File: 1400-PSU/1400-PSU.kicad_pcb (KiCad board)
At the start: 2 copper layers, 173.4 x 62.1 mm, 42 parts, among them J1 Battery, J2 Charger, J3 MAINBOARD_OUT, Q1 IRF9540N, SW1 SW_DPST, U3 LM7805_TO220, U4 7812

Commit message: Generated gerbers.
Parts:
- added F1: 3A, Fuse:Fuseholder_Blade_Mini_Keystone_3568, F.Cu at (86.0, 76.7)
- added G***: LOGO, Logo:Logo-15mm, F.Cu at (192.6, 98.8)
- added NT1: NetTie_2, NetTie:NetTie-2_SMD_Pad2.0mm, F.Cu at (92.6, 93.0)
- added NT2: NetTie_2, NetTie:NetTie-2_SMD_Pad2.0mm, F.Cu at (88.2, 102.9)
- added NT3: NetTie_2, NetTie:NetTie-2_SMD_Pad2.0mm, F.Cu at (112.2, 92.9)
- C1: footprint Capacitor_THT:CP_Radial_D10.0mm_P5.00mm -> Capacitor_THT:CP_Radial_D8.0mm_P3.50mm
- C3: footprint Capacitor_THT:C_Disc_D4.7mm_W2.5mm_P5.00mm -> Capacitor_THT:C_Disc_D5.1mm_W3.2mm_P5.00mm
- C4: value 22uF 25V -> 0.1uF; footprint Capacitor_THT:CP_Radial_D6.3mm_P2.50mm -> Capacitor_THT:C_Disc_D5.1mm_W3.2mm_P5.00mm
- C8: value 10uF 50V -> 0.22uF; footprint Capacitor_THT:CP_Radial_D8.0mm_P5.00mm -> Capacitor_THT:C_Disc_D5.1mm_W3.2mm_P5.00mm
- J2: value Charger -> Jack-DC
- U3: footprint Package_TO_SOT_THT:TO-220-3_Vertical -> Package_TO_SOT_THT:TO-220-3_Horizontal_TabDown
- U4: value 7812 -> LM340T-12; footprint Package_TO_SOT_THT:TO-220-3_Vertical -> Package_TO_SOT_THT:TO-220-3_Horizontal_TabDown
- U5: value ~ -> N7812-1PH; footprint Package_TO_SOT_THT:TO-220-3_Vertical -> Package_TO_SOT_THT:TO-220-3_Horizontal_TabDown
- moved R1 84.2 mm to (92.3, 84.0), turned to 0 degrees
- moved R2 84.0 mm to (92.5, 88.2), turned to 0 degrees
- moved U2 82.0 mm to (180.6, 58.5)
- moved R8 81.9 mm to (165.2, 73.1)
- moved R9 81.9 mm to (175.1, 73.1)
- moved JP1 55.3 mm to (184.9, 117.3), turned to -90 degrees
- moved C8 54.5 mm to (113.7, 102.6)
- moved C7 41.0 mm to (148.6, 105.8), turned to 180 degrees
- moved C6 39.4 mm to (158.7, 112.8)
- moved U3 35.3 mm to (153.6, 106.7), turned to 0 degrees
- moved R6 31.8 mm to (119.9, 67.5)
- moved RV1 29.7 mm to (130.3, 68.8)
- moved U4 28.8 mm to (118.8, 107.0), turned to 0 degrees
- moved C2 27.2 mm to (96.1, 78.6)
- moved R4 26.7 mm to (119.9, 71.3)
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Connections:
- D1 pad 2: BATT_SENSE -> Net-(D1-A)
- J2 pad 1: GND -> Net-(F1-Pad2)
- J2 pad 2: POWER_BRICK -> GND
- Q1 pad 2: BATT_SENSE -> Net-(D1-A)
- R1 pad 2: POWER_BRICK -> Net-(NT1-Pad2)
- R2 pad 1: POWER_BRICK -> Net-(NT1-Pad2)
- R8 pad 1: POWER_BRICK -> CHARGER_SENSE
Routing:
- net 15_RAIL: track 144.3 -> 238.7 mm, vias 1 -> 0
- net Net-(A1-A1): track 136.5 -> 45.5 mm, vias 3 -> 0
- net POWER_BRICK: track 146.6 -> 58.4 mm, vias 1 -> 0
- net Net-(Q1-G): track 104.7 -> 27.2 mm, vias 3 -> 0
- net Net-(JP2-A): track 101.0 -> 39.3 mm
- net CHARGER_SENSE: track 0.00 -> 59.4 mm, vias 0 -> 1
- net 5_RAIL: track 74.0 -> 33.7 mm
- net Net-(D1-K): track 139.5 -> 110.0 mm, vias 8 -> 0
- net ARDUINO_5V: track 25.4 -> 52.9 mm, vias 0 -> 1
- net Net-(D1-A): track 0.00 -> 25.8 mm
- net 12_RAIL: track 88.5 -> 65.1 mm
- net LOW_BATT: track 40.6 -> 20.6 mm, vias 2 -> 0
- net BATT_SENSE: track 106.0 -> 86.2 mm, vias 2 -> 1
- net REALLY_LOW_BATT: track 41.3 -> 22.1 mm, vias 2 -> 0
- net STANDBY: track 43.4 -> 24.5 mm, vias 2 -> 0
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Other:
- board text added: "-12V_RAIL"
- board text added: "-22V_RAIL"
- board text added: "12V_RAIL"
- board text added: "5V_RAIL"
- board text added: "ALWAYS_ON_5V"
- board text added: "GND"
- board text added: "LOW_BATT"
- board text added: "NOT_CONNECTED"
- board text added: "ON_CHARGER"
- board text added: "OPTIONAL TP5100 CHARGER"
- board text added: "PWR_ON"
- board text added: "REALLY_LOW_BATT"
- board text added: "STANDBY"
- board text added: "TANDY 1400FD/HD PSU REAPLCEMENT"

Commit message: Updating for next board revision.
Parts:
- removed REF** (x4): MountingHole_3.5mm_Pad_TopBottom, MountingHole:MountingHole_3.5mm_Pad_TopBottom
- added H1: ~, MountingHole:MountingHole_3.5mm_Pad_TopBottom, F.Cu at (222.4, 63.6)
- added H2: ~, MountingHole:MountingHole_3.5mm_Pad_TopBottom, F.Cu at (197.5, 117.7)
- added H3: ~, MountingHole:MountingHole_3.5mm_Pad_TopBottom, F.Cu at (62.0, 115.1)
- added H4: ~, MountingHole:MountingHole_3.5mm_Pad_TopBottom, F.Cu at (74.7, 66.5)
- added JP3: LOW_BATT, Jumper:SolderJumper-2_P1.3mm_Open_RoundedPad1.0x1.5mm, F.Cu at (196.6, 81.6)
- added JP4: REALLY_LOW_BATT, Jumper:SolderJumper-2_P1.3mm_Open_RoundedPad1.0x1.5mm, F.Cu at (199.2, 81.6)
- C2: value 220uF 50V -> 47uF 50V
- D1: value 1N4001 -> 31DQ06; footprint Diode_THT:D_DO-41_SOD81_P10.16mm_Horizontal -> Diode_THT:D_DO-201AD_P5.08mm_Vertical_AnodeUp
- D2: value 1N4001 -> 31D106; footprint Diode_THT:D_DO-41_SOD81_P10.16mm_Horizontal -> Diode_THT:D_DO-201AD_P5.08mm_Vertical_KathodeUp
- D4: value 1N4001 -> 31DQ06; footprint Diode_THT:D_DO-41_SOD81_P10.16mm_Horizontal -> Diode_THT:D_DO-201AD_P12.70mm_Horizontal
- R4: value 1k -> 20k
- R6: value 20k -> 1k
- moved D1 9.03 mm to (76.6, 87.6), turned to 90 degrees
- moved RV1 5.59 mm to (125.0, 67.0), turned to 90 degrees
- moved L1 4.59 mm to (109.1, 67.4), turned to 180 degrees
- moved D2 4.58 mm to (84.9, 87.7), turned to 90 degrees
- moved NT3 4.50 mm to (109.0, 89.7)
- moved J1 3.46 mm to (62.2, 91.9), turned to -90 degrees
- moved D4 3.44 mm to (67.5, 94.2)
- moved U2 1.78 mm to (181.5, 60.0)
- moved A1 0.60 mm to (188.7, 87.0)
- moved R9 0.55 mm to (175.0, 73.6)
- moved R8 0.54 mm to (165.1, 73.6)
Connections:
- C3 pad 2: GND -> -22_RAIL
- L1 pad 1: Net-(D3-K) -> GND
- L1 pad 2: Net-(U1-Switch_Emiiter) -> Net-(D3-K)
- U1 pad 2: Net-(U1-Switch_Emiiter) -> Net-(D3-K)
- U1 pad 4: GND -> -22_RAIL
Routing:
- net -22_RAIL: track 115.2 -> 143.8 mm
- net Net-(U1-Switch_Emiiter): track 22.9 -> 0.00 mm, vias 1 -> 0
- net Net-(D3-K): track 4.94 -> 25.4 mm, vias 0 -> 1
- net Net-(A1-VIN): track 43.2 -> 61.0 mm, vias 1 -> 2
- net Net-(D1-A): track 25.8 -> 35.1 mm
- net POWER_BRICK: track 58.4 -> 50.9 mm
- net 15_RAIL: track 238.7 -> 231.5 mm
- net Net-(D1-K): track 110.0 -> 116.4 mm
- net REALLY_LOW_BATT: track 22.1 -> 28.0 mm
- net LOW_BATT: track 20.6 -> 23.3 mm
- net BATT_SENSE: track 86.2 -> 88.8 mm, vias 1 -> 3
- net Net-(JP2-A): track 39.3 -> 41.2 mm
- net CHARGER_SENSE: track 59.4 -> 60.8 mm
- net BATT_POS: track 19.6 -> 20.9 mm
- net Net-(D4-A): track 4.49 -> 5.67 mm
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
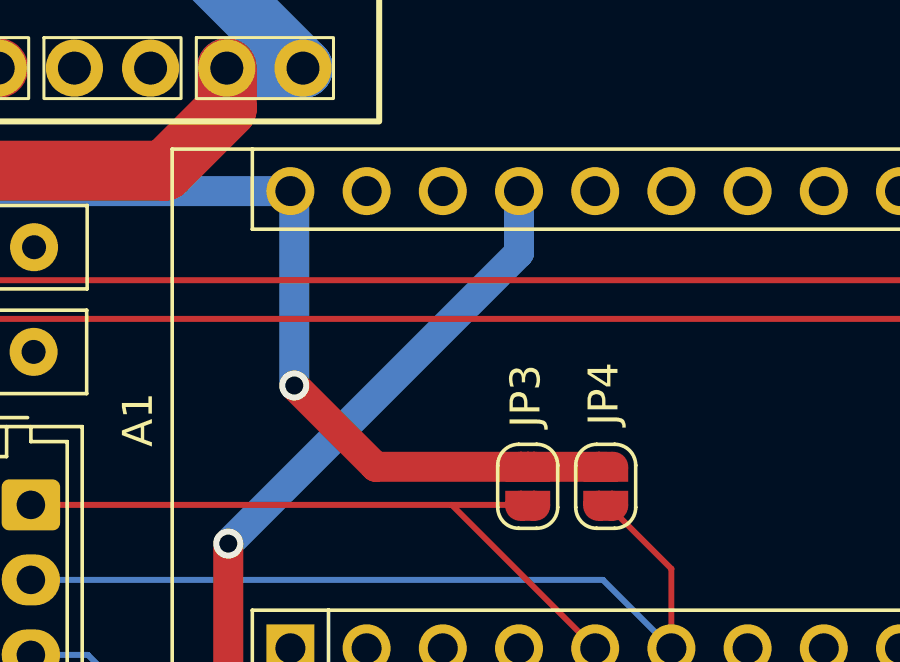
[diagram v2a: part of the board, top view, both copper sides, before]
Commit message: Update to readme and BOM.
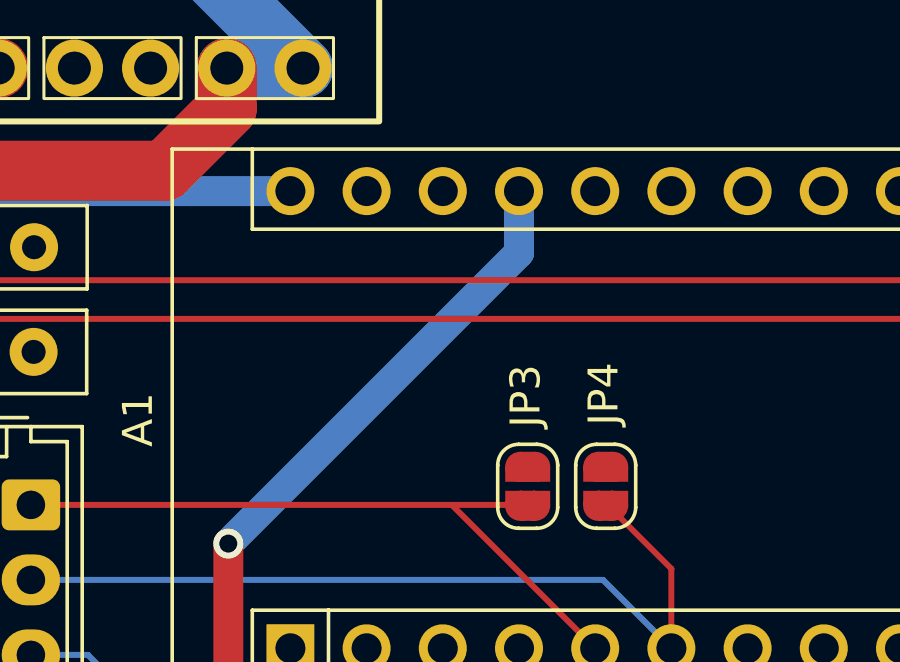
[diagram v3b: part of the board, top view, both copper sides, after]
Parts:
- U1: value ~ -> MC34063
- U2: value ~ -> MEZD41502A-C
- U3: value LM7805_TO220 -> MEZD72401A-G
- U6: value ~ -> TP5100 Module
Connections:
- JP3 pad 2: Net-(A1-VIN) -> GND
- JP4 pad 2: Net-(A1-VIN) -> GND
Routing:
- net Net-(A1-VIN): track 61.0 -> 43.1 mm, vias 2 -> 1
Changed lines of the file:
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@@
 		(tags "Inductor Radial series Radial pin pitch 5.00mm  diameter 8.7mm Fastron 07HCP")
 		(property "Reference" "L1"
-			(at 2.5 -5.6 360)
+			(at 2.5 -5.6 0)
 			(layer "F.SilkS")
 			(effects
@@
 		)
 		(property "Value" "330uH"
-			(at 2.5 5.6 360)
+			(at 2.5 5.6 0)
 			(layer "F.Fab")
 			(effects
@@
 		)
 		(fp_text user "${REFERENCE}"
-			(at 2.5 0 360)
+			(at 2.5 0 0)
 			(layer "F.Fab")
 			(effects
@@
 			(size 1 0.5)
 			(layers "F.Cu" "F.Mask")
-			(net 46 "Net-(A1-VIN)")
+			(net 7 "GND")
 			(pinfunction "B")
 			(pintype "passive")
@@
 			(size 1 0.5)
 			(layers "F.Cu" "F.Mask")
-			(net 46 "Net-(A1-VIN)")
+			(net 7 "GND")
 			(pinfunction "B")
 			(pintype "passive")
@@
 			)
 		)
-		(property "Value" "~"
+		(property "Value" "MC34063"
 			(at -0.508 9.398 0)
 			(layer "F.Fab")
@@
 			)
 		)
-		(property "Value" "~"
+		(property "Value" "MEZD41502A-C"
 			(at 0.762 3.302 0)
 			(unlocked yes)
@@
 			)
 		)
-		(property "Value" "~"
+		(property "Value" "TP5100 Module"
 			(at 0 1 0)
 			(unlocked yes)
@@
 			)
 		)
-		(property "Value" "LM7805_TO220"
+		(property "Value" "MEZD72401A-G"
 			(at 2.54 2 0)
 			(layer "F.Fab")
@@
 	)
 	(segment
-		(start 191.51 80.96)
-		(end 188.8 78.25)
-		(width 1)
-		(layer "F.Cu")
-		(net 46)
-	)
-	(segment
 		(start 151.29 80.01)
 		(end 151.29 78.17)
@@
 	)
 	(segment
-		(start 196.58 80.96)
-		(end 191.51 80.96)
-		(width 1)
-		(layer "F.Cu")
-		(net 46)
-	)
-	(segment
 		(start 151.18 80.12)
 		(end 151.29 80.01)
@@
 		(net 46)
 	)
-	(segment
-		(start 196.58 80.96)
-		(end 199.18 80.96)
-		(width 1)
-		(layer "F.Cu")
-		(net 46)
-	)
-	(via
-		(at 188.8 78.25)
-		(size 1)
-		(drill 0.6)
-		(layers "F.Cu" "B.Cu")
-		(net 46)
-	)
 	(via
 		(at 151.18 80.12)
@@
 		(width 1)
 		(layer "B.Cu")
-		(net 46)
-	)
-	(segment
-		(start 188.8 78.25)
-		(end 188.8 71.9)
-		(width 1)
-		(layer "B.Cu")

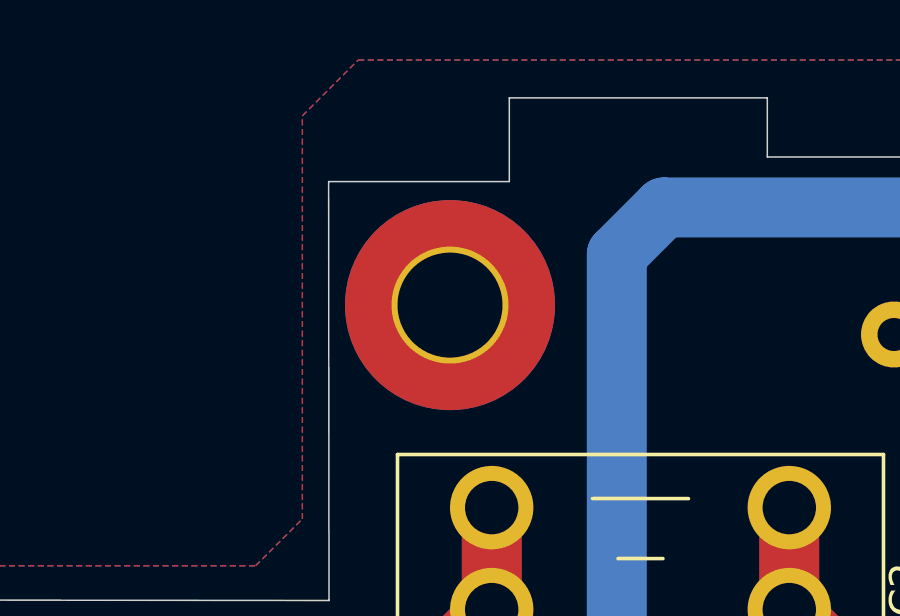
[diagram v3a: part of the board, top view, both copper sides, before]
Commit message: Move one of the mounting holes a bit.
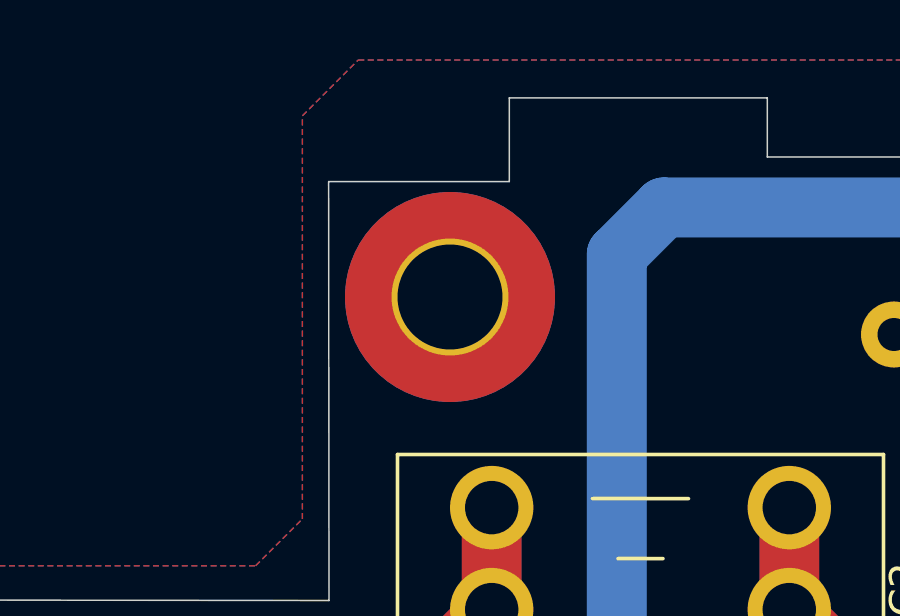
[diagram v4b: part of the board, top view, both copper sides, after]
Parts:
- moved H4 0.27 mm to (74.7, 66.2)
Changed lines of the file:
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@@
 	(footprint "MountingHole:MountingHole_3.5mm_Pad_TopBottom"
 		(layer "F.Cu")
-		(at 74.69 66.52)
+		(at 74.69 66.25)
 		(descr "Mounting Hole 3.5mm")
 		(tags "mounting hole 3.5mm")

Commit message: Minor revisions.
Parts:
- added C10: 330uF 25V, Capacitor_THT:CP_Radial_D8.0mm_P5.00mm, F.Cu at (95.4, 88.4)
- J1: footprint Connector_JST:JST_EH_B2B-EH-A_1x02_P2.50mm_Vertical -> Connector_Wire:SolderWire-1.5sqmm_1x02_P7.8mm_D1.7mm_OD3.9mm
- R4: value 20k -> 15k
- moved D2 22.7 mm to (89.6, 65.5), turned to -90 degrees
- moved R1 22.0 mm to (74.5, 97.0)
- moved D1 21.9 mm to (82.5, 66.5), turned to -90 degrees
- moved SW1 16.3 mm to (151.3, 75.8), turned to 180 degrees
- moved R2 13.9 mm to (79.5, 93.1), turned to 180 degrees
- moved U2 13.2 mm to (172.6, 69.9), turned to 180 degrees
- moved C8 12.7 mm to (123.9, 110.3)
- moved D3 12.7 mm to (108.0, 77.1), turned to -90 degrees
- moved U1 12.0 mm to (122.5, 77.1)
- moved C3 11.9 mm to (113.6, 81.5)
- moved C7 11.7 mm to (154.2, 116.1), turned to -90 degrees
- moved C1 11.5 mm to (136.2, 80.4), turned to 90 degrees
- moved R3 11.2 mm to (128.7, 75.4)
- moved R4 9.70 mm to (129.1, 68.4)
- moved D4 9.67 mm to (74.7, 87.7)
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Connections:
- SW1 pad 1: Net-(D1-K) -> Net-(JP2-A)
- SW1 pad 2: Net-(JP2-A) -> Net-(D1-K)
- SW1 pad 3: Net-(D1-K) -> Net-(JP2-A)
- SW1 pad 4: Net-(JP2-A) -> Net-(D1-K)
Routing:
- net 15_RAIL: track 231.5 -> 160.9 mm, vias 0 -> 1
- net Net-(D1-K): track 116.4 -> 82.3 mm
- net -22_RAIL: track 143.8 -> 124.0 mm, vias 1 -> 2
- net POWER_BRICK: track 50.9 -> 66.0 mm
- net Net-(Q1-G): track 27.2 -> 12.2 mm
- net Net-(D1-A): track 35.1 -> 41.7 mm, vias 0 -> 1
- net Net-(D3-K): track 25.4 -> 19.6 mm
- net BATT_POS: track 20.9 -> 26.5 mm
- net -12_RAIL: track 54.6 -> 49.5 mm
- net CHARGER_SENSE: track 60.8 -> 56.1 mm
- net Net-(U1-Comparator_Inverting_Input): track 24.1 -> 20.4 mm
- net BATT_SENSE: track 88.8 -> 85.8 mm, vias 3 -> 1
- net Net-(NT1-Pad2): track 9.43 -> 11.5 mm
- net Net-(F1-Pad2): track 11.3 -> 9.35 mm
- net 12_RAIL: track 65.1 -> 63.2 mm
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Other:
- outline, holes or cut-outs redrawn

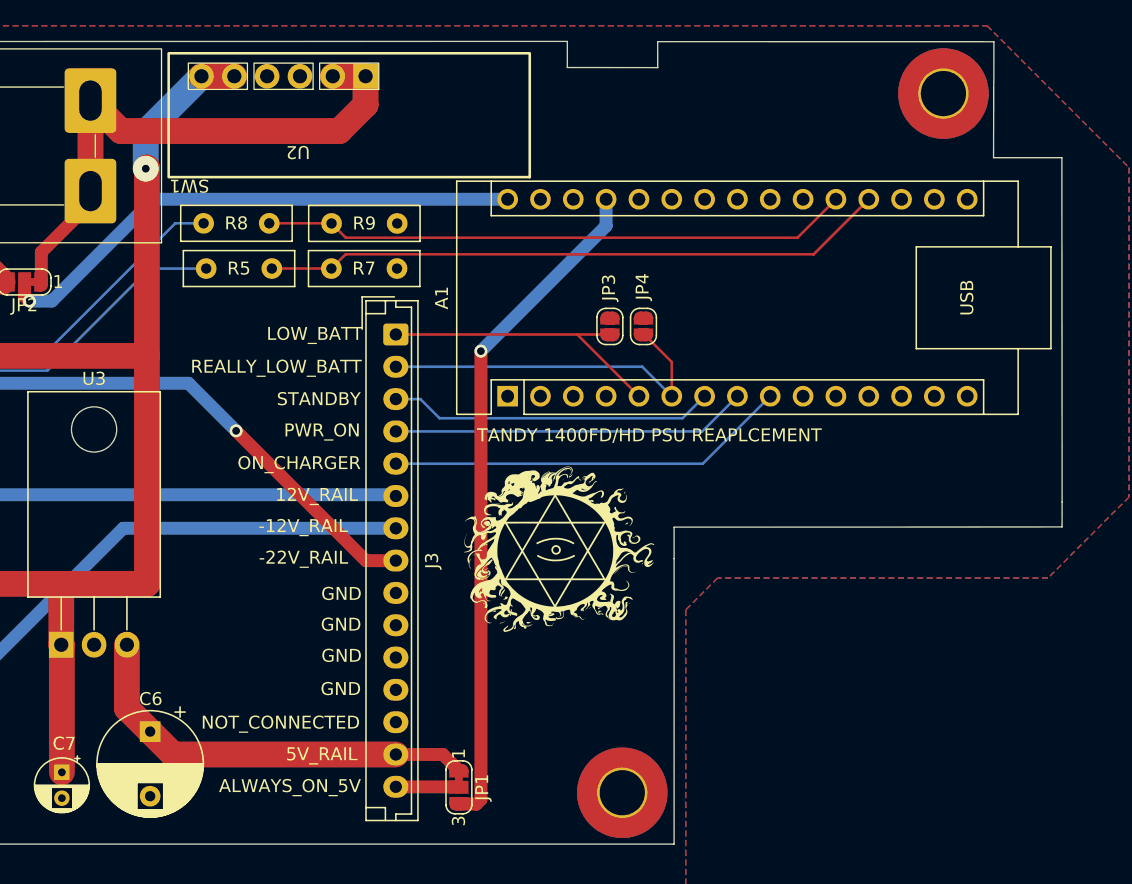
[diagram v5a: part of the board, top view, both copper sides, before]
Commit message: Should fix #4.
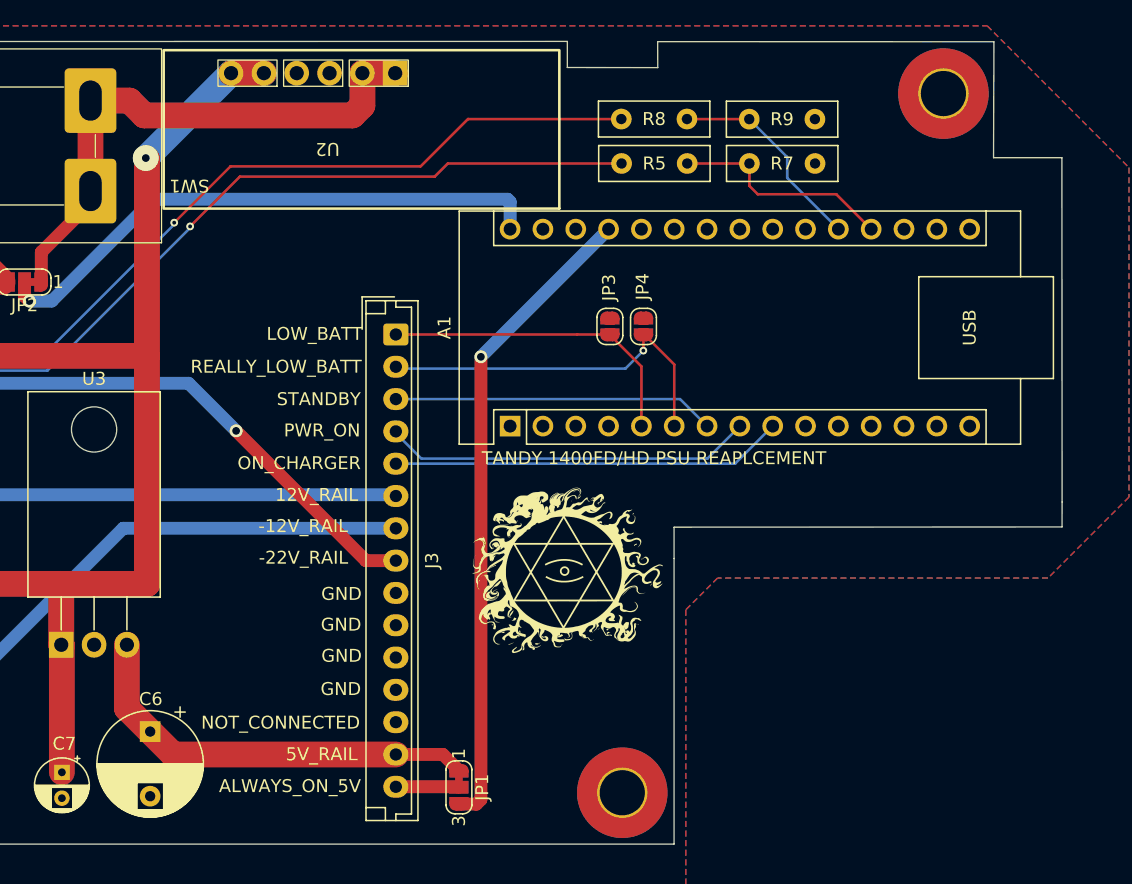
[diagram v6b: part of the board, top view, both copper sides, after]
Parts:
- moved R7 33.4 mm to (207.4, 69.0)
- moved R9 33.3 mm to (207.4, 65.6)
- moved R8 33.3 mm to (197.5, 65.6)
- moved R5 33.2 mm to (197.5, 69.0)
- moved A1 2.32 mm to (188.9, 89.3)
- moved U2 2.30 mm to (174.9, 69.6)
- moved G*** 1.77 mm to (193.3, 100.5)
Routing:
- net CHARGER_SENSE: track 56.1 -> 91.9 mm, vias 1 -> 2
- net BATT_SENSE: track 85.8 -> 121.4 mm, vias 1 -> 2
- net Net-(A1-A0): track 48.4 -> 17.4 mm
- net Net-(A1-A1): track 45.5 -> 16.2 mm
- net 15_RAIL: track 160.9 -> 164.4 mm
- net ARDUINO_5V: track 52.3 -> 50.1 mm
- net Net-(A1-VIN): track 42.1 -> 44.3 mm
- net Net-(JP2-A): track 42.6 -> 44.1 mm
- net LOW_BATT: track 23.3 -> 24.6 mm
- net REALLY_LOW_BATT: track 28.0 -> 29.1 mm, vias 0 -> 1
- net PWR_ON: track 27.6 -> 28.6 mm
- net ON_CHARGER: track 31.1 -> 30.4 mm

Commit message: Adjust battery warning voltage dividers.
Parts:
- R5, R8: value 10k -> 200k
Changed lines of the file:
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@@
 			)
 		)
-		(property "Value" "10k"
+		(property "Value" "200k"
 			(at 2.54 2.52 0)
 			(layer "F.Fab")
@@
 			)
 		)
-		(property "Value" "10k"
+		(property "Value" "200k"
 			(at 2.54 2.52 0)
 			(layer "F.Fab")

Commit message: Minor update and fixes.
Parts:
- C2: value 47uF 50V -> 100uF 50V
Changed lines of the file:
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@@
 			)
 		)
-		(property "Value" "47uF 50V"
+		(property "Value" "100uF 50V"
 			(at 2.5 6.25 0)
 			(layer "F.Fab")
